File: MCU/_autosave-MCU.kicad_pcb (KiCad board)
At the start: 2 copper layers, 105.5 x 79 mm, 78 parts, among them J2 Conn_01x02, J3 Conn_01x02, J4 Conn_01x02, J5 Conn_01x02, J6 Conn_01x04, U1 Nucleo_L432KC, U3 HHG1D-1, U4 AMC3302QDWERQ1, U5 HHG1D-1, U6 AMC3302QDWERQ1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

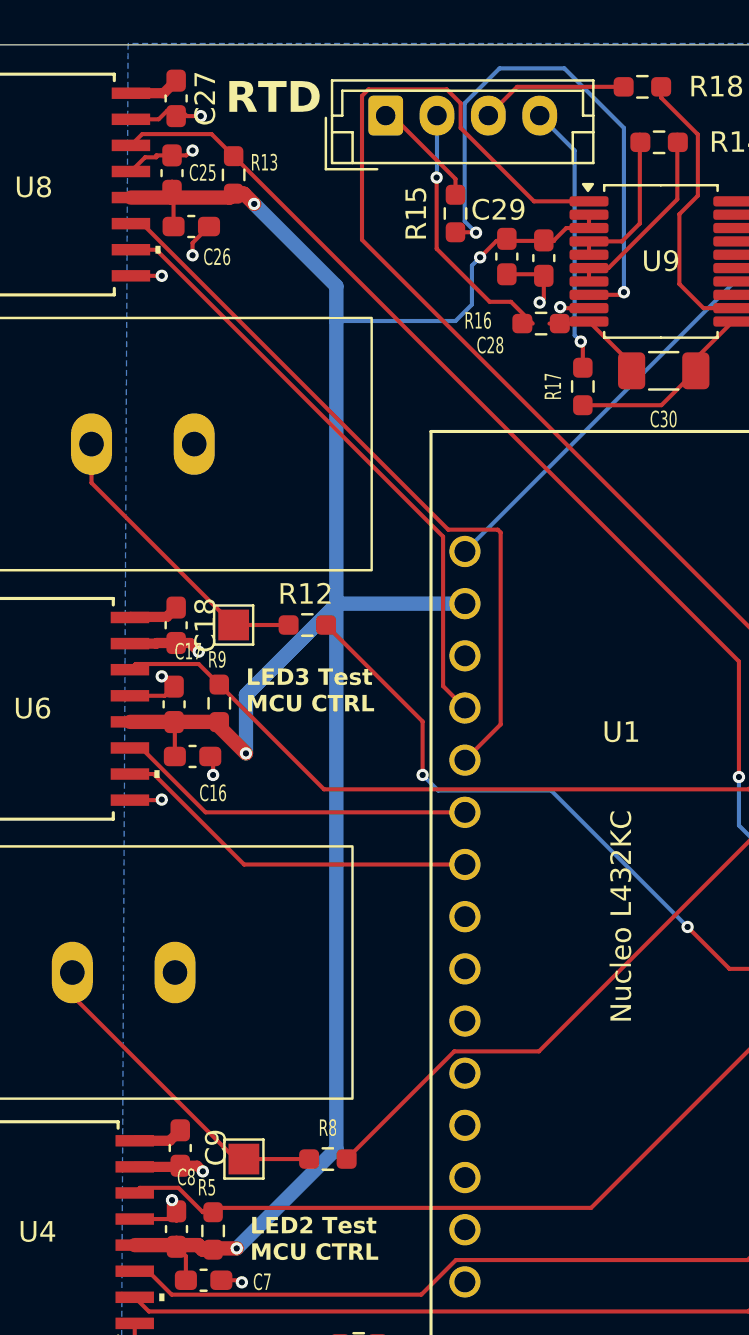
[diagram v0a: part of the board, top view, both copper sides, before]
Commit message: fixed ferrite bead size
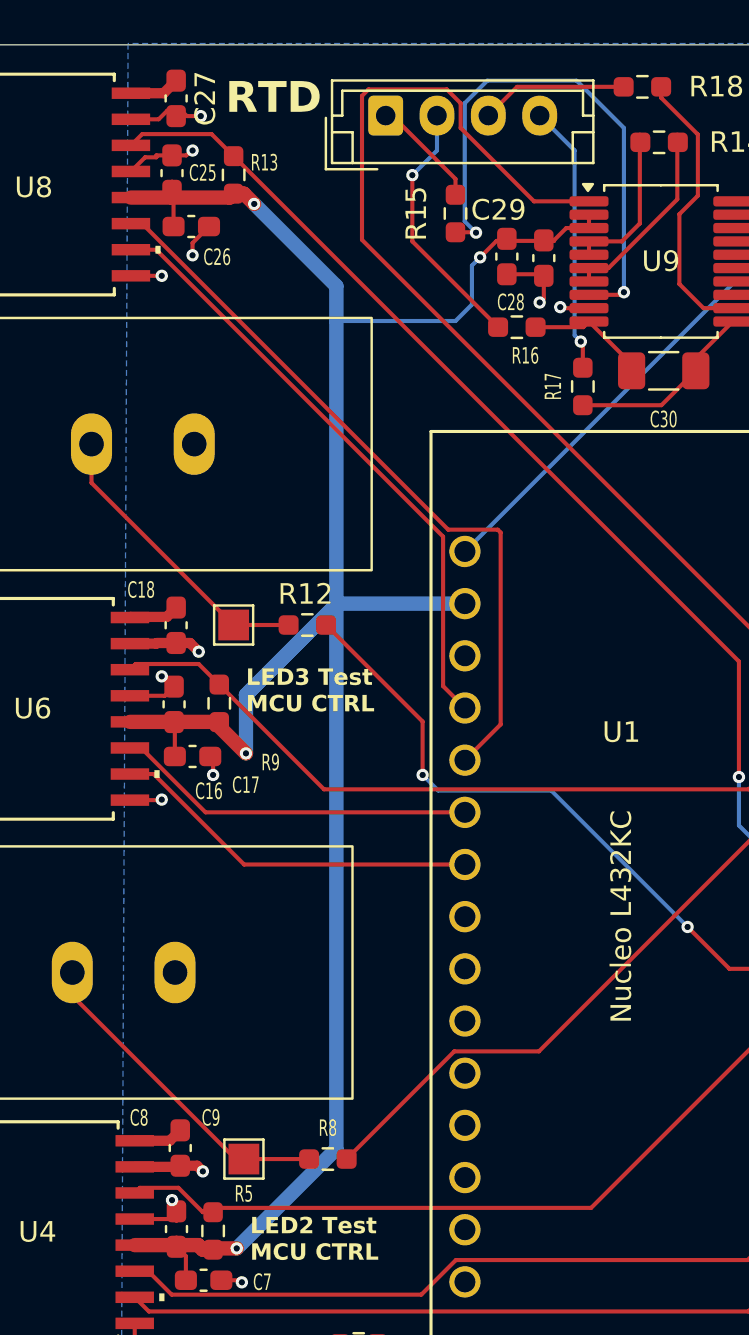
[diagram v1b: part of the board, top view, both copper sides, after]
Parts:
- moved R16 1.19 mm to (171.3, 65.0)
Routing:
- net Net-(U9-RTDIN+): track 5.23 -> 5.97 mm
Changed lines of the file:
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@@
 		(tags "capacitor handsolder")
 		(property "Reference" "C28"
-			(at -4.2625 -2.6 180)
+			(at -2.1625 -1.6 180)
 			(layer "F.SilkS")
 			(effects
@@
 		(tags "resistor handsolder")
 		(property "Reference" "R5"
-			(at -2.1 0.3 180)
+			(at -1.8 -1.5 180)
 			(layer "F.SilkS")
 			(effects
@@
 		(tags "capacitor handsolder")
 		(property "Reference" "C9"
-			(at -0.0225 -1.74875 270)
+			(at -1.4625 -1.5 0)
 			(layer "F.SilkS")
 			(effects
 				(font
-					(size 1 1)
-					(thickness 0.15)
+					(size 0.8 0.5)
+					(thickness 0.08)
 				)
 			)
@@
 	(footprint "Resistor_SMD:R_0603_1608Metric_Pad0.98x0.95mm_HandSolder"
 		(layer "F.Cu")
-		(at 172.4675 64.825 180)
+		(at 171.2875 65 180)
 		(descr "Resistor SMD 0603 (1608 Metric), square (rectangular) end terminal, IPC-7351 nominal with elongated pad for handsoldering. (Body size source: IPC-SM-782 page 72, https://www.pcb-3d.com/wordpress/wp-content/uploads/ipc-sm-782a_amendment_1_and_2.pdf), generated with kicad-footprint-generator")
 		(tags "resistor handsolder")
 		(property "Reference" "R16"
-			(at 3.0675 0.125 180)
+			(at -0.4125 -1.4 180)
 			(layer "F.SilkS")
 			(effects
@@
 		(tags "capacitor handsolder")
 		(property "Reference" "C8"
-			(at 2.5075 0.4827 180)
+			(at 5.4075 -1.8173 180)
 			(layer "F.SilkS")
 			(effects
@@
 		(tags "resistor handsolder")
 		(property "Reference" "R9"
-			(at -2.1125 0.1 180)
+			(at 2.8875 -2.5 180)
 			(layer "F.SilkS")
 			(effects
@@
 		(tags "capacitor handsolder")
 		(property "Reference" "C17"
-			(at 2.5625 0.7 180)
+			(at -3.9375 3.5 180)
 			(layer "F.SilkS")
 			(effects
@@
 		(tags "capacitor handsolder")
 		(property "Reference" "C18"
-			(at 0 -1.43 270)
+			(at -1.713237 1.7 0)
 			(layer "F.SilkS")
 			(effects
 				(font
-					(size 1 1)
-					(thickness 0.15)
+					(size 0.8 0.5)
+					(thickness 0.08)
 				)
 			)
@@
 		(tags "capacitor handsolder")
 		(property "Reference" "C16"
-			(at 1 1.8 0)
+			(at 0.8 1.7 0)
 			(layer "F.SilkS")
 			(effects
@@
 	)
 	(segment
-		(start 172.875 64.825)
-		(end 174.7 64.825)
+		(start 174.525 65)
+		(end 174.8 64.725)
 		(width 0.2)
 		(layer "F.Cu")
@@
 	)
 	(segment
-		(start 174.7 64.825)
-		(end 174.8 64.725)
+		(start 172.2 65)
+		(end 174.525 65)
 		(width 0.2)
 		(layer "F.Cu")
@@
 	)
 	(segment
-		(start 169.965 63.765)
-		(end 171 63.765)
-		(width 0.2)
-		(layer "F.Cu")
-		(net 69)
-	)
-	(segment
-		(start 171 63.765)
-		(end 172.06 64.825)
+		(start 170.375 65)
+		(end 166.2 60.825)
 		(width 0.2)
 		(layer "F.Cu")
@@
 	)
 	(segment
-		(start 167.383235 61.183235)
-		(end 169.965 63.765)
-		(width 0.2)
-		(layer "F.Cu")
-		(net 69)
-	)
-	(segment
-		(start 167.383235 57.716765)
-		(end 167.383235 61.183235)
+		(start 166.2 60.825)
+		(end 166.2 57.6)
 		(width 0.2)
 		(layer "F.Cu")
@@
 	)
 	(via
-		(at 167.383235 57.716765)
+		(at 166.2 57.6)
 		(size 0.6)
 		(drill 0.3)
@@
 	)
 	(segment
-		(start 167.4 57.7)
+		(start 167.4 56.4)
 		(end 167.4 54.7)
 		(width 0.2)
@@
 	)
 	(segment
-		(start 167.383235 57.716765)
-		(end 167.4 57.7)
+		(start 166.2 57.6)
+		(end 167.4 56.4)
 		(width 0.2)
 		(layer "B.Cu")
@@
 	)
 	(segment
-		(start 169.3 60.4)
-		(end 168.749 59.849)
+		(start 169.84724 53)
+		(end 174.2 53)
 		(width 0.2)
 		(layer "B.Cu")
@@
 	)
 	(segment
-		(start 176.5 55.3)
-		(end 176.5 63.3)
+		(start 174.2 53)
+		(end 176.5 55.3)
 		(width 0.2)
 		(layer "B.Cu")
@@
 	)
 	(segment
-		(start 168.749 54.09824)
-		(end 170.44724 52.4)
+		(start 176.5 55.3)
+		(end 176.5 63.3)
 		(width 0.2)
 		(layer "B.Cu")
@@
 	)
 	(segment
-		(start 170.44724 52.4)
-		(end 173.6 52.4)
+		(start 168.749 54.09824)
+		(end 169.84724 53)
 		(width 0.2)
 		(layer "B.Cu")
@@
 	)
 	(segment
-		(start 173.6 52.4)
-		(end 176.5 55.3)
+		(start 169.3 60.4)
+		(end 168.749 59.849)
 		(width 0.2)
 		(layer "B.Cu")
